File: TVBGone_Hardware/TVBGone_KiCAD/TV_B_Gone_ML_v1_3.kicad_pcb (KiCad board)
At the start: 2 copper layers, 55 x 33 mm, 22 parts, among them IC1 ATTINY85, P1 BATTERY, P2 ISP, P3 PCB, Q1 BC640, Q2 BC548, Q3 BC548, Q4 BC548, Q5 BC548, SW1 START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

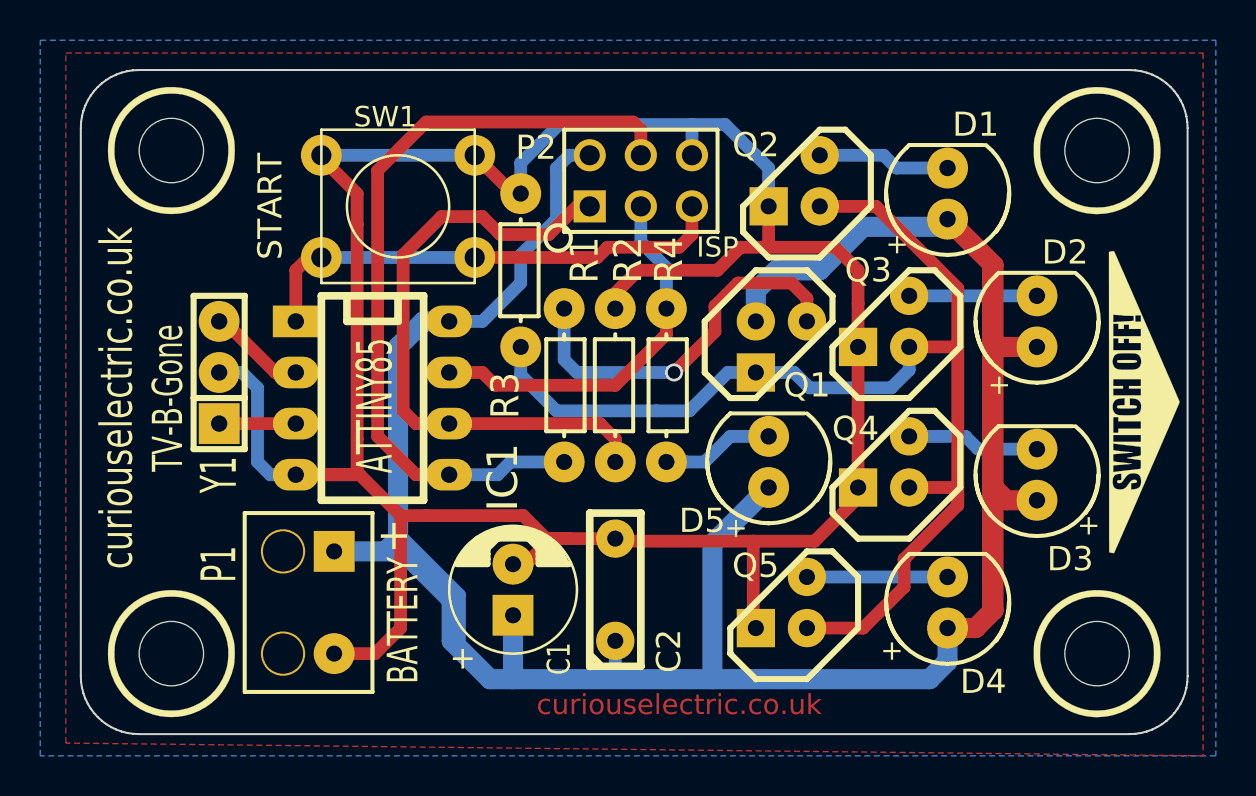
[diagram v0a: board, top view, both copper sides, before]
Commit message: Updates to Kicad 9 and sorted schematic
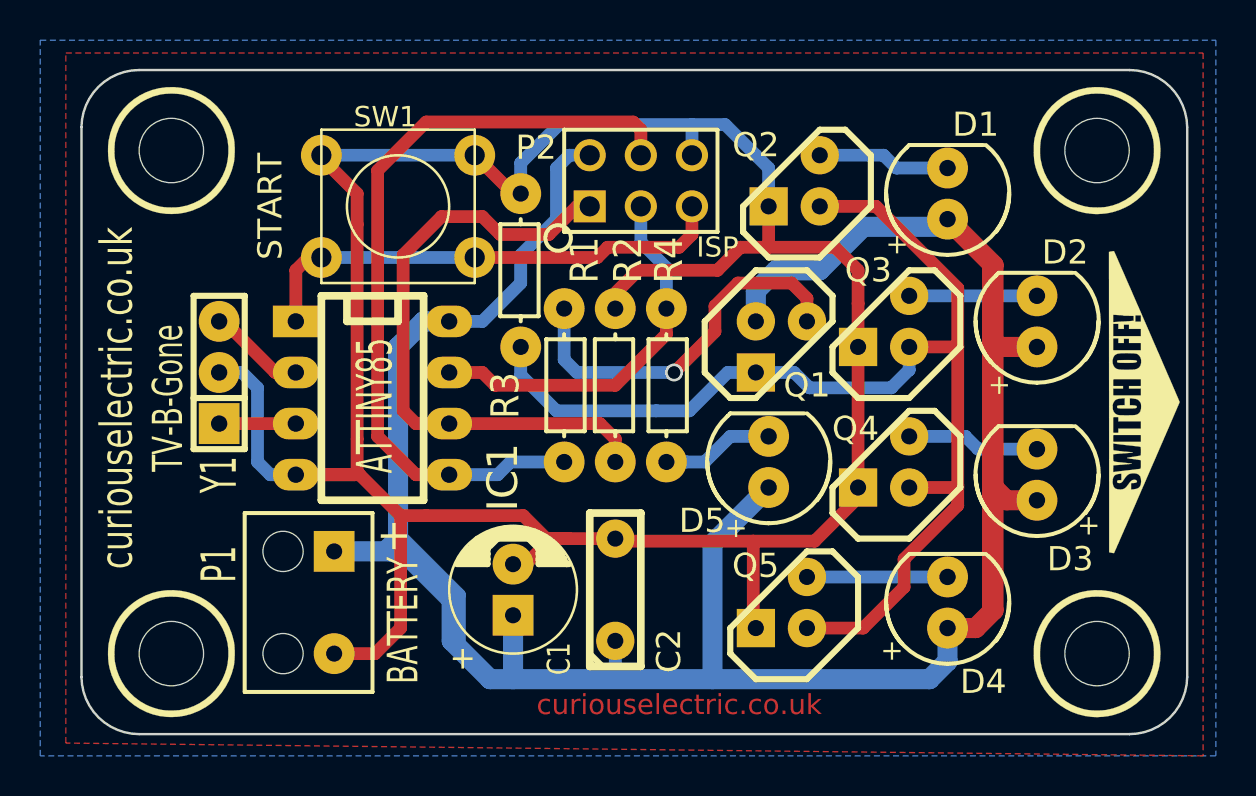
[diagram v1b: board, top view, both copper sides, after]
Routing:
- net VCC: track 198.1 -> 164.9 mm
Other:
- board size 55 x 33 mm -> 54.9 x 33 mm
- net class 15 removed
- net class 20 removed
- net class 30 removed
- net class 50 removed
- net class Default removed
